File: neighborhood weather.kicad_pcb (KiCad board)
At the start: 2 copper layers, 56 x 56 mm, 3 parts, among them U1 AM2302

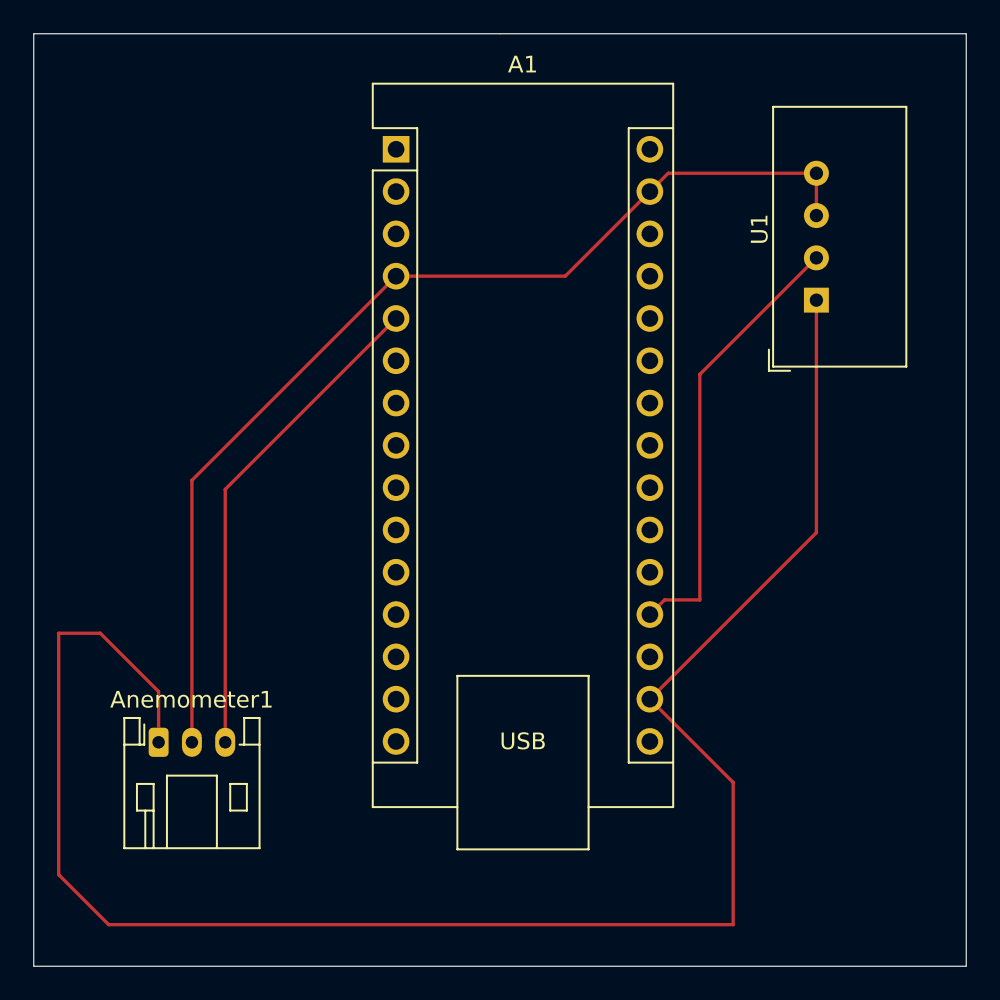
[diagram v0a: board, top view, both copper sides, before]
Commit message: added a barometric pressure/altitude sensor <bmp180> and updated wiring
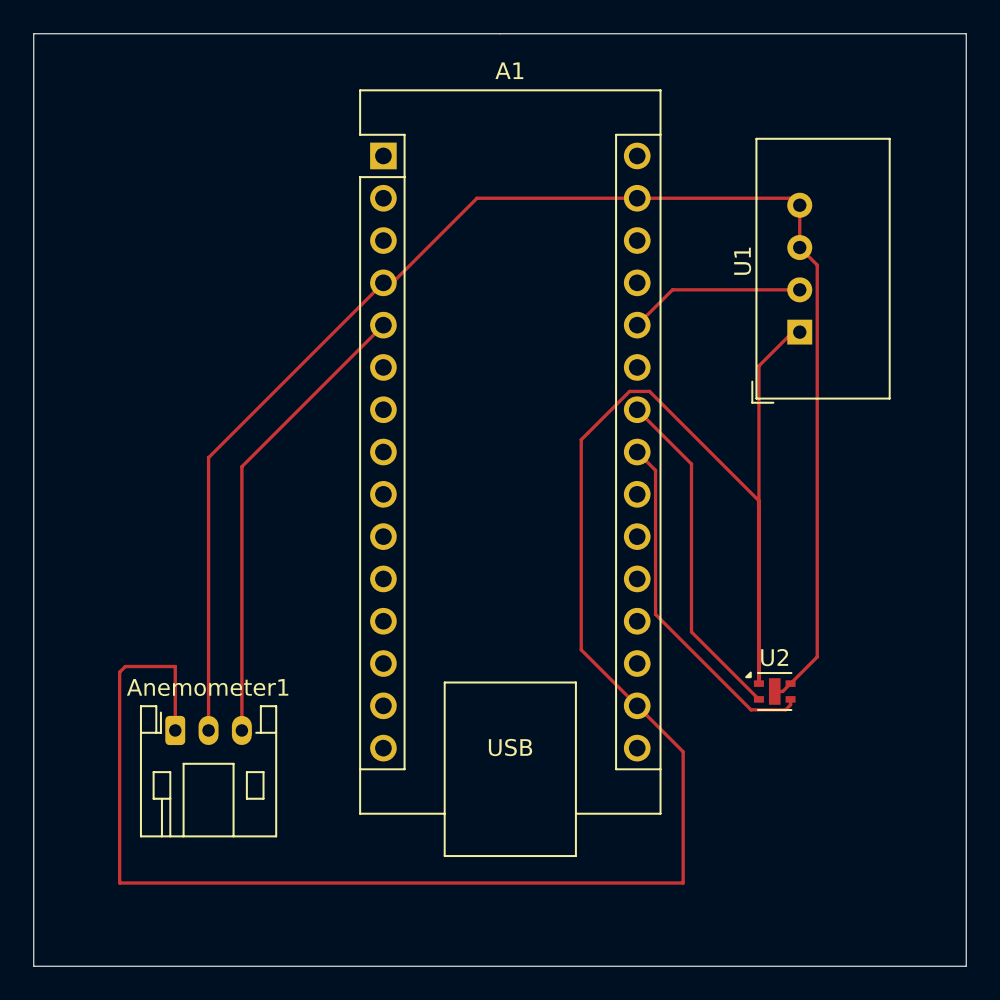
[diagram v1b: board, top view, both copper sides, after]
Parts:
- added U2: ENS210, Package_DFN_QFN:AMS_QFN-4-1EP_2x2mm_P0.95mm_EP0.7x1.6mm, F.Cu at (142.0, 97.5)
- moved U1 2.16 mm to (143.5, 75.9)
- moved Anemometer1 1.23 mm to (106.0, 99.8)
- moved A1 0.86 mm to (118.5, 65.3)
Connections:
- A1 pad 19: Net-(A1-A0) -> unconnected-(A1-A0-Pad19)
- A1 pad 23: unconnected-(A1-SDA/A4-Pad23) -> Net-(A1-SDA/A4)
- A1 pad 24: unconnected-(A1-SCL/A5-Pad24) -> Net-(A1-SCL/A5)
- A1 pad 26: unconnected-(A1-A7-Pad26) -> Net-(A1-A7)
- U1 pad 2: Net-(A1-A0) -> Net-(A1-A7)
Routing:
- net Net-(A1-A0): track 26.8 -> 0.00 mm
- net Net-(Anemometer1-GND): track 63.4 -> 89.5 mm
- net Net-(A1-SDA/A4): track 0.00 -> 21.1 mm
- net Net-(A1-3V3): track 110.5 -> 130.9 mm
- net Net-(A1-SCL/A5): track 0.00 -> 20.4 mm
- net Net-(A1-A7): track 0.00 -> 10.6 mm
- net Net-(A1-D2): track 29.7 -> 27.9 mm
